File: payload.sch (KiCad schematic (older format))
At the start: 26 parts, among them J11 JST-PA-2, J12 JST-PA-2, J14 JST-PA-2, J15 JST-PA-2, J23 JST-PA-2, J24 JST-PA-2, Q5 IRFZ44, Q6 IRFZ44, U14 74LS74, U15 74LS74

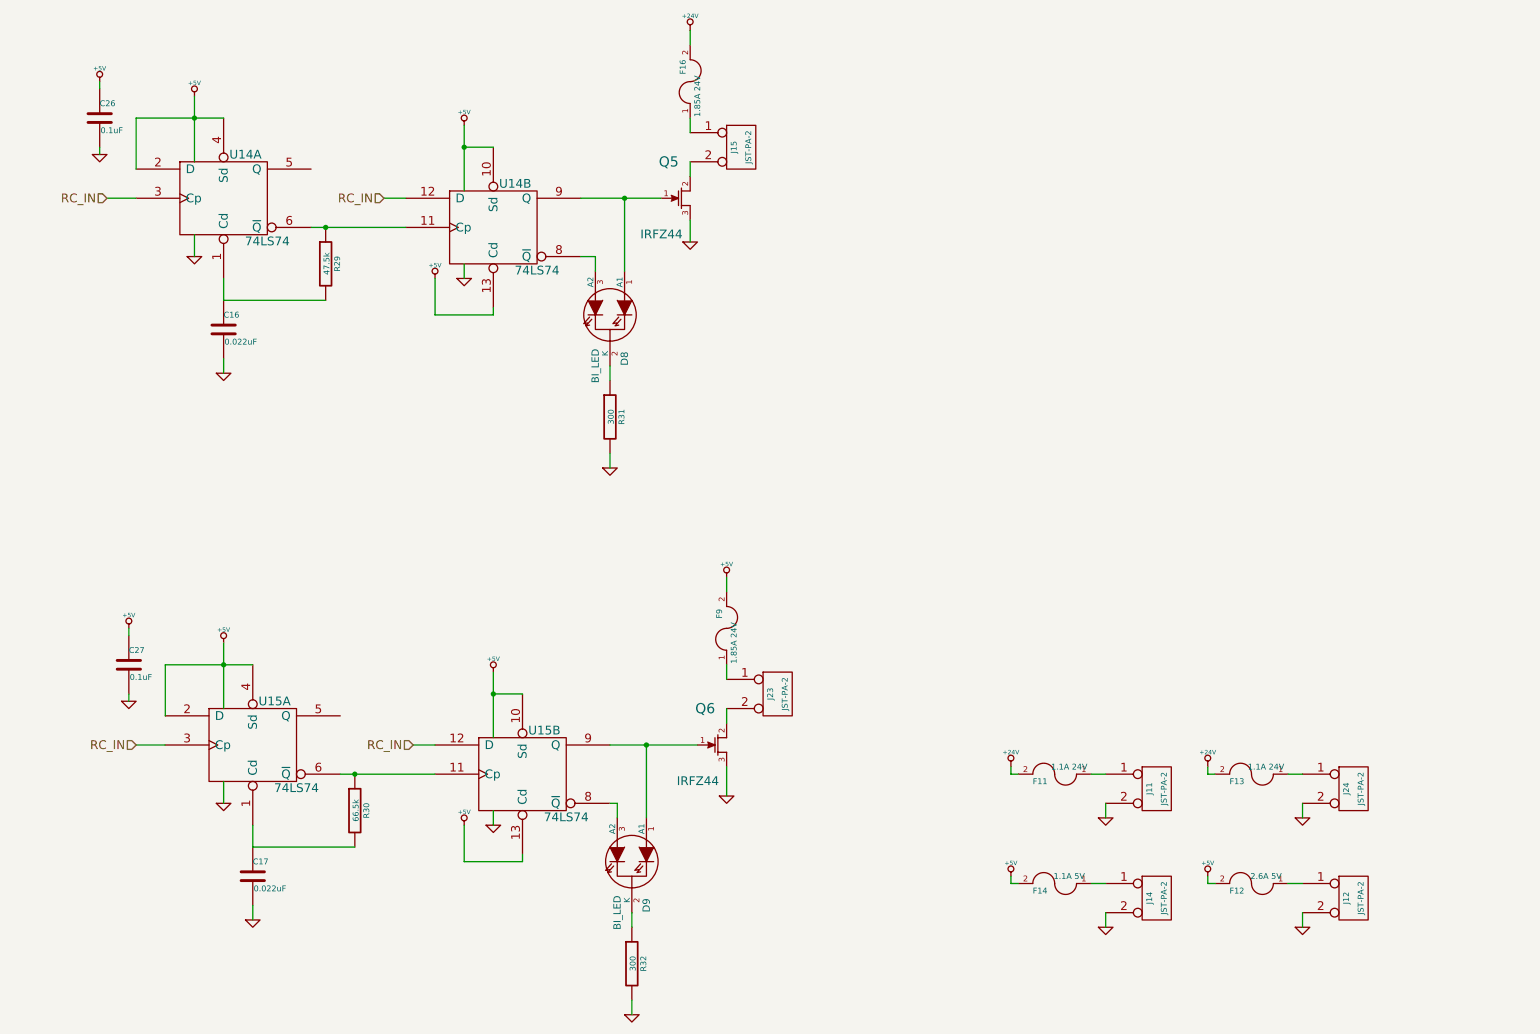
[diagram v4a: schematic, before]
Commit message: Updating design with new 12v bus.
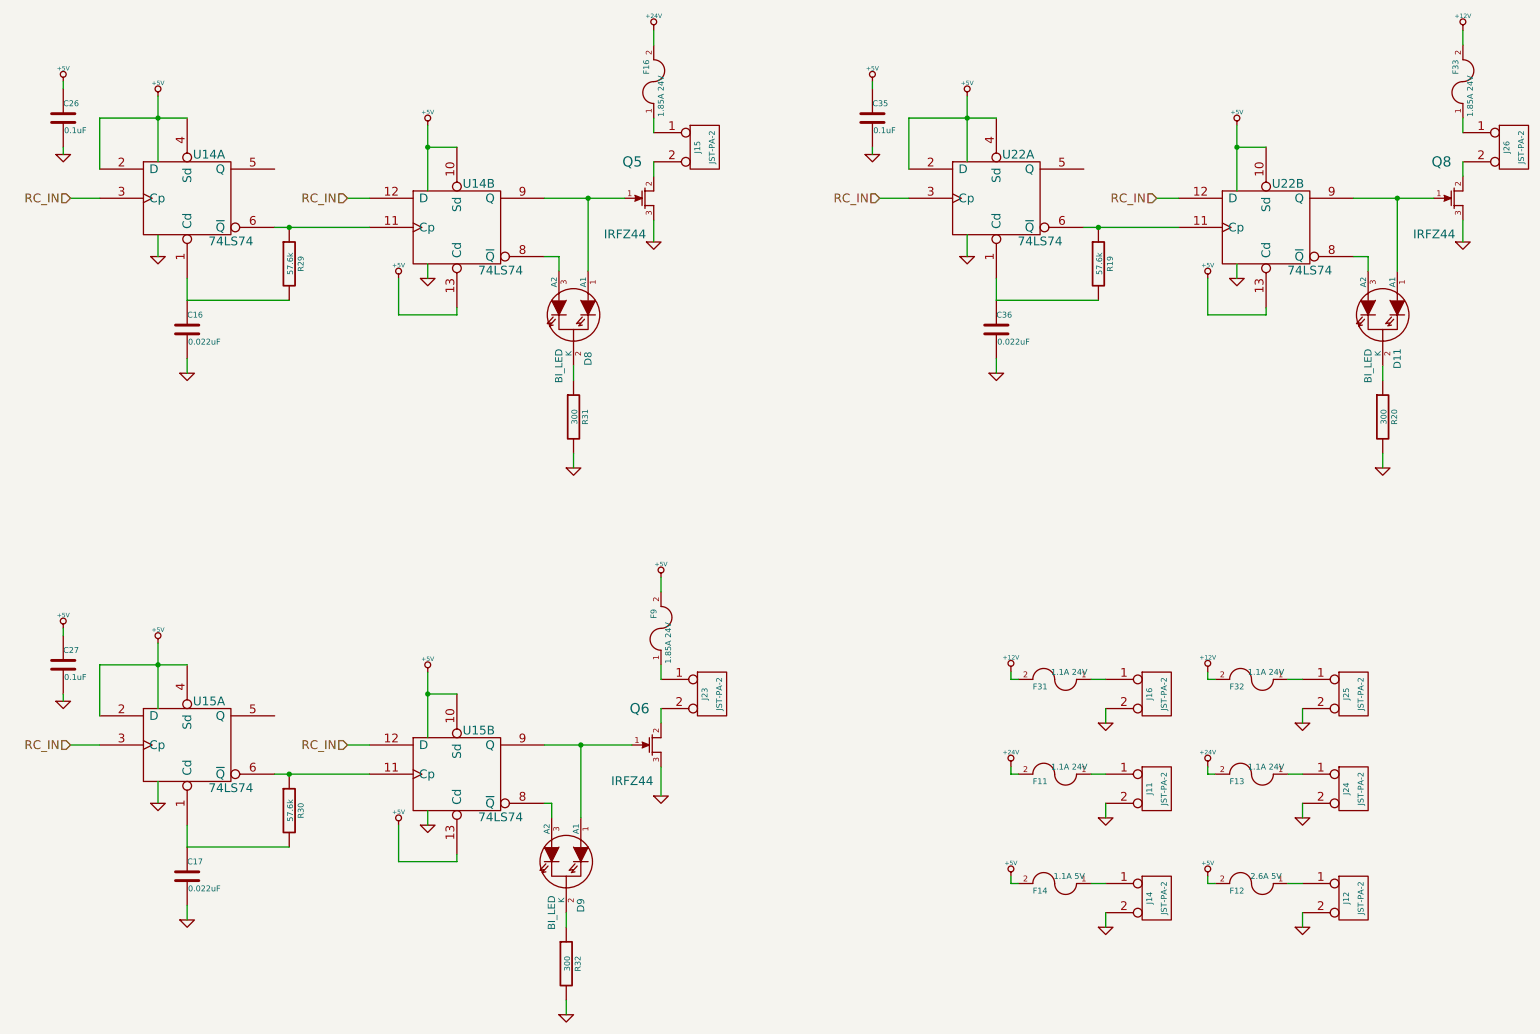
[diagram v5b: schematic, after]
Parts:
- added C35: 0.1uF, SM0805, symbol C
- added C36: 0.022uF, ~, symbol C
- added D11: BI_LED, ~, symbol BI_LED
- added F31, F32: 1.1A 24V, ~, symbol FUSE
- added F33: 1.85A 24V, ~, symbol FUSE
- added J16, J25, J26: JST-PA-2, ~, symbol CONN_2
- added Q8: IRFZ44, ~, symbol FET_N_GDS
- added R19: 57.6k, ~, symbol R
- added R20: 300, ~, symbol R
- added U22: 74LS74, ~, symbol 74LS74
- R29: value 47.5k -> 57.6k; Digikey P47.5KDACT-ND -> P57.6KDACT-ND
- R30: value 66.5k -> 57.6k; Digikey P66.5KDACT-ND -> P57.6KDACT-ND
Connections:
- net +5V: now also C35.1, U22.10 (Sd), U22.13 (Cd), U22.14 (VCC), U22.14 (VCC), U22.2 (D), U22.4 (Sd)
- net GND: now also C35.2, C36.2, J16.2 (PM), J25.2 (PM), Q8.3 (S), R20.2, U22.7 (GND), U22.7 (GND)
- net RC_IN: now also U22.12 (D), U22.3 (Cp)
- new net: C36.1, R19.2, U22.1 (Cd)
- new net: R19.1, U22.11 (Cp), U22.6 (~Q)
- new net: D11.3 (A2), U22.8 (~Q)
- new net: D11.1 (A1), Q8.1 (G), U22.9 (Q)
- new net: J26.2 (PM), Q8.2 (D)
- new net: D11.2 (K), R20.1
- new net: F33.1, J26.1 (P1)
- new net: F32.1, J25.1 (P1)
- new net: F31.1, J16.1 (P1)
- new net +12V: F31.2, F32.2, F33.2
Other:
- moved on the sheet: C16, C17, C26, C27, D8, D9, F16, F9, J15, J23, Q5, Q6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

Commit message: Preliminary layout complete.
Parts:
- removed C17, C36: 0.022uF, ~, symbol C
- removed C27, C35: 0.1uF, SM0805, symbol C
- removed D11, D9: BI_LED, ~, symbol BI_LED
- removed R19, R30: 57.6k, ~, symbol R
- removed R20, R32: 300, ~, symbol R
- removed U15, U22: 74LS74, ~, symbol 74LS74
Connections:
- net Payload_Switched: now reaches Q6.1 (G)
- net Payload_Switched: now also D8.1 (A1), Q5.1 (G), Q8.1 (G), U14.9 (Q)
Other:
- moved on the sheet: C16, C26, D8, F16, F33, F9, J15, J23, J26, Q5, Q6, Q8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
